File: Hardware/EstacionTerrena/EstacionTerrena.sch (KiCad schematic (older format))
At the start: 10 parts, among them J1 5-1814832-1

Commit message: Corrección de librerías en PCB de estación terrena
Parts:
- removed J1: 5-1814832-1, SamacSys_Parts:5-1814832-1, symbol EstacionTerrena-rescue:5-1814832-1-SamacSys_Parts
- removed JP1: Jumper_NC_Dual, Jumper:SolderJumper-3_P1.3mm_Open_RoundedPad1.0x1.5mm_NumberLabels, symbol Device:Jumper_NC_Dual
- added J1: 5-1814832-1, 5-1814832-1, symbol SamacSys_Parts:5-1814832-1
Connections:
- wire segments 29 -> 25
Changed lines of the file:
@@
 EESchema Schematic File Version 4
 LIBS:EstacionTerrena-cache
-EELAYER 26 0
+EELAYER 29 0
 EELAYER END
 $Descr A4 11693 8268
@@
 $EndComp
 Wire Wire Line
-	7050 4050 6700 4050
-$Comp
-L EstacionTerrena-rescue:5-1814832-1-SamacSys_Parts J1
-U 1 1 5BEE5678
-P 7250 4050
-F 0 "J1" H 7491 4026 50  0000 L CNN
-F 1 "5-1814832-1" H 7491 3934 50  0000 L CNN
-F 2 "SamacSys_Parts:5-1814832-1" H 7650 4150 50  0001 L CNN
-F 3 "http://www.te.com/commerce/DocumentDelivery/DDEController?Action=srchrtrv&DocNm=1814832&DocType=Customer+Drawing&DocLang=English" H 7650 4050 50  0001 L CNN
-F 4 "SUBMINIATURE COAX" H 7650 3950 50  0001 L CNN "Description"
-F 5 "TE Connectivity" H 7650 3750 50  0001 L CNN "Manufacturer_Name"
-F 6 "5-1814832-1" H 7650 3650 50  0001 L CNN "Manufacturer Part Number"
-F 7 "1355074" H 7450 3550 50  0001 L CNN "RS Part Number"
-F 8 "http://uk.rs-online.com/web/p/products/1355074" H 7650 3450 50  0001 L CNN "RS Price/Stock"
-F 9 "70084637" H 7650 3350 50  0001 L CNN "Allied_Number"
-F 10 "https://www.alliedelec.com/te-connectivity-5-1814832-1/70084637/" H 7650 3250 50  0001 L CNN "Allied Price/Stock"
-F 11 "5-1814832-1" H 7650 3150 50  0001 L CNN "Arrow Part Number"
-F 12 "https://www.arrow.com/en/products/5-1814832-1/te-connectivity" H 7650 3050 50  0001 L CNN "Arrow Price/Stock"
-	1    7250 4050
-	1    0    0    -1
-$EndComp
-Wire Wire Line
 	7150 4250 7150 4300
 Wire Wire Line
@@
 	1    0    0    -1
 $EndComp
-$Comp
-L power:GND #PWR026
-U 1 1 5C00A55B
-P 6050 5050
-F 0 "#PWR026" H 6050 4800 50  0001 C CNN
-F 1 "GND" H 6055 4877 50  0000 C CNN
-F 2 "" H 6050 5050 50  0001 C CNN
-F 3 "" H 6050 5050 50  0001 C CNN
-	1    6050 5050
-	1    0    0    -1
-$EndComp
 Wire Wire Line
 	5100 3950 5200 3950
@@
 $EndComp
 Wire Wire Line
-	5600 4250 6100 4250
-Wire Wire Line
 	5100 4250 5350 4250
 Wire Wire Line
@@
 Wire Wire Line
 	5200 3950 6100 3950
-$Comp
-L Device:Jumper_NC_Dual JP1
-U 1 1 5C2DD6B3
-P 5600 4950
-F 0 "JP1" H 5600 5096 50  0000 C CNN
-F 1 "Jumper_NC_Dual" H 5600 5187 50  0000 C CNN
-F 2 "Jumper:SolderJumper-3_P1.3mm_Open_RoundedPad1.0x1.5mm_NumberLabels" H 5600 4950 50  0001 C CNN
-F 3 "~" H 5600 4950 50  0001 C CNN
-	1    5600 4950
-	-1   0    0    1
-$EndComp
-Wire Wire Line
-	5350 4950 5350 4250
-Connection ~ 5350 4250
-Wire Wire Line
-	5600 4250 5600 4850
-Wire Wire Line
-	5850 4950 6050 4950
-Wire Wire Line
-	6050 4950 6050 5050
 Wire Wire Line
 	5100 4050 5250 4050
@@
 EndData
 $EndBitmap
+Wire Wire Line
+	5350 4250 6100 4250
+Connection ~ 5350 4250
+Wire Wire Line
+	7050 4050 6700 4050
+$Comp
+L SamacSys_Parts:5-1814832-1 J1
+U 1 1 5CCF549E
+P 7250 4050
+F 0 "J1" H 7494 4025 50  0000 L CNN
+F 1 "5-1814832-1" H 7494 3934 50  0000 L CNN
+F 2 "5-1814832-1" H 7650 4150 50  0001 L CNN
+F 3 "http://www.te.com/commerce/DocumentDelivery/DDEController?Action=srchrtrv&DocNm=1814832&DocType=Customer+Drawing&DocLang=English" H 7650 4050 50  0001 L CNN
+F 4 "SUBMINIATURE COAX" H 7650 3950 50  0001 L CNN "Description"
+F 5 "TE Connectivity" H 7650 3750 50  0001 L CNN "Manufacturer_Name"
+F 6 "5-1814832-1" H 7650 3650 50  0001 L CNN "Manufacturer Part Number"
+F 7 "1355074" H 7450 3550 50  0001 L CNN "RS Part Number"
+F 8 "http://uk.rs-online.com/web/p/products/1355074" H 7650 3450 50  0001 L CNN "RS Price/Stock"
+F 9 "70084637" H 7650 3350 50  0001 L CNN "Allied_Number"
+F 10 "https://www.alliedelec.com/te-connectivity-5-1814832-1/70084637/" H 7650 3250 50  0001 L CNN "Allied Price/Stock"
+F 11 "5-1814832-1" H 7650 3150 50  0001 L CNN "Arrow Part Number"
+F 12 "https://www.arrow.com/en/products/5-1814832-1/te-connectivity" H 7650 3050 50  0001 L CNN "Arrow Price/Stock"
+	1    7250 4050
+	1    0    0    -1
+$EndComp
 $EndSCHEMATC

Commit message: Estacion terrena:
- Nuevo LDO de 500mA para poder utilizar el CC1190 a toda su potencia de ser necesario
- Cambiado el MCP2210 por un PIC18F14K50 ya que el MCP2210 es MUY lento para transferencias SPI
- Agregado de footprints faltantes
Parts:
- J1: footprint 5-1814832-1 -> SamacSys_Parts:5-1814832-1
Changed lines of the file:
@@
 F 0 "J1" H 7494 4025 50  0000 L CNN
 F 1 "5-1814832-1" H 7494 3934 50  0000 L CNN
-F 2 "5-1814832-1" H 7650 4150 50  0001 L CNN
+F 2 "SamacSys_Parts:5-1814832-1" H 7650 4150 50  0001 L CNN
 F 3 "http://www.te.com/commerce/DocumentDelivery/DDEController?Action=srchrtrv&DocNm=1814832&DocType=Customer+Drawing&DocLang=English" H 7650 4050 50  0001 L CNN
 F 4 "SUBMINIATURE COAX" H 7650 3950 50  0001 L CNN "Description"

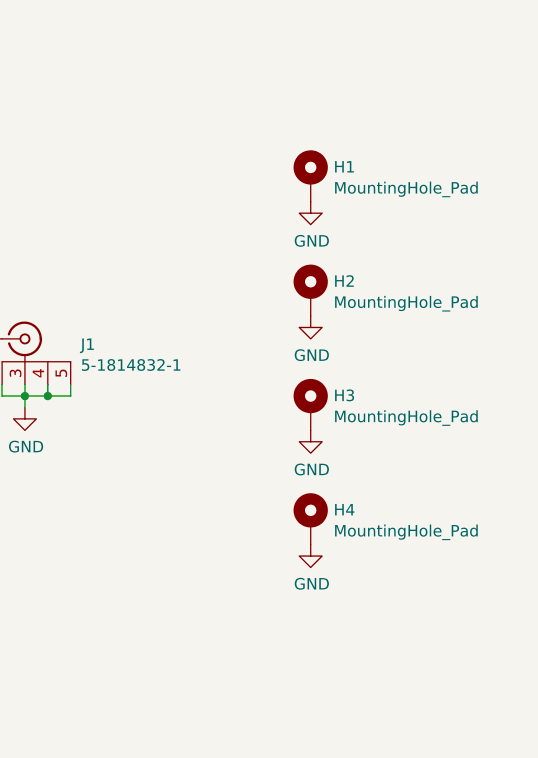
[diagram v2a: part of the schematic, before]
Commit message: Nuevo PCB de estación terrena con CC1190
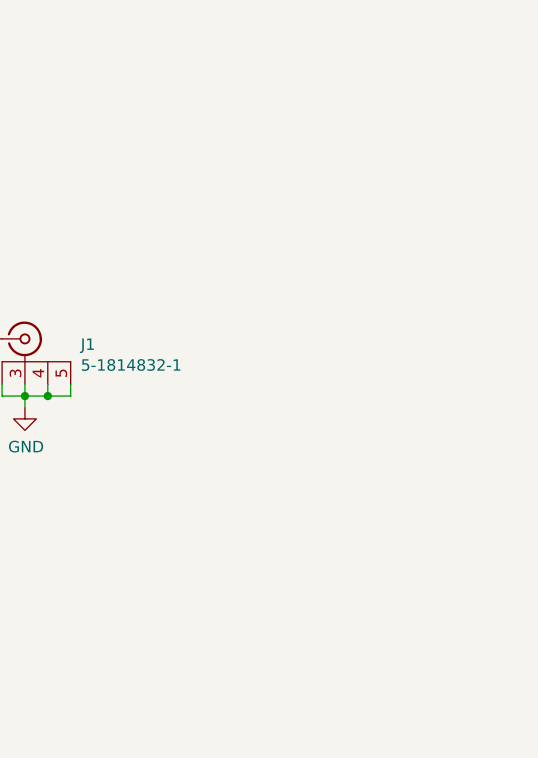
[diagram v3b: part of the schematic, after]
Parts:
- removed H1, H2, H3, H4: MountingHole_Pad, MountingHole:MountingHole_3.2mm_M3_Pad, symbol Mechanical:MountingHole_Pad
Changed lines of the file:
@@
 	7250 4350 7250 4300
-$Comp
-L Mechanical:MountingHole_Pad H1
-U 1 1 5BBFD953
-P 8500 3350
-F 0 "H1" H 8600 3401 50  0000 L CNN
-F 1 "MountingHole_Pad" H 8600 3309 50  0000 L CNN
-F 2 "MountingHole:MountingHole_3.2mm_M3_Pad" H 8500 3350 50  0001 C CNN
-F 3 "~" H 8500 3350 50  0001 C CNN
-	1    8500 3350
-	1    0    0    -1
-$EndComp
-$Comp
-L Mechanical:MountingHole_Pad H2
-U 1 1 5BBFDA3A
-P 8500 3850
-F 0 "H2" H 8600 3901 50  0000 L CNN
-F 1 "MountingHole_Pad" H 8600 3809 50  0000 L CNN
-F 2 "MountingHole:MountingHole_3.2mm_M3_Pad" H 8500 3850 50  0001 C CNN
-F 3 "~" H 8500 3850 50  0001 C CNN
-	1    8500 3850
-	1    0    0    -1
-$EndComp
-$Comp
-L Mechanical:MountingHole_Pad H3
-U 1 1 5BBFDA66
-P 8500 4350
-F 0 "H3" H 8600 4401 50  0000 L CNN
-F 1 "MountingHole_Pad" H 8600 4309 50  0000 L CNN
-F 2 "MountingHole:MountingHole_3.2mm_M3_Pad" H 8500 4350 50  0001 C CNN
-F 3 "~" H 8500 4350 50  0001 C CNN
-	1    8500 4350
-	1    0    0    -1
-$EndComp
-$Comp
-L Mechanical:MountingHole_Pad H4
-U 1 1 5BBFDA96
-P 8500 4850
-F 0 "H4" H 8600 4901 50  0000 L CNN
-F 1 "MountingHole_Pad" H 8600 4809 50  0000 L CNN
-F 2 "MountingHole:MountingHole_3.2mm_M3_Pad" H 8500 4850 50  0001 C CNN
-F 3 "~" H 8500 4850 50  0001 C CNN
-	1    8500 4850
-	1    0    0    -1
-$EndComp
-$Comp
-L power:GND #PWR0101
-U 1 1 5BBFDACC
-P 8500 3450
-F 0 "#PWR0101" H 8500 3200 50  0001 C CNN
-F 1 "GND" H 8505 3277 50  0000 C CNN
-F 2 "" H 8500 3450 50  0001 C CNN
-F 3 "" H 8500 3450 50  0001 C CNN
-	1    8500 3450
-	1    0    0    -1
-$EndComp
-$Comp
-L power:GND #PWR0102
-U 1 1 5BBFDAE9
-P 8500 3950
-F 0 "#PWR0102" H 8500 3700 50  0001 C CNN
-F 1 "GND" H 8505 3777 50  0000 C CNN
-F 2 "" H 8500 3950 50  0001 C CNN
-F 3 "" H 8500 3950 50  0001 C CNN
-	1    8500 3950
-	1    0    0    -1
-$EndComp
-$Comp
-L power:GND #PWR0103
-U 1 1 5BBFDB80
-P 8500 4450
-F 0 "#PWR0103" H 8500 4200 50  0001 C CNN
-F 1 "GND" H 8505 4277 50  0000 C CNN
-F 2 "" H 8500 4450 50  0001 C CNN
-F 3 "" H 8500 4450 50  0001 C CNN
-	1    8500 4450
-	1    0    0    -1
-$EndComp
-$Comp
-L power:GND #PWR0104
-U 1 1 5BBFDB9D
-P 8500 4950
-F 0 "#PWR0104" H 8500 4700 50  0001 C CNN
-F 1 "GND" H 8505 4777 50  0000 C CNN
-F 2 "" H 8500 4950 50  0001 C CNN
-F 3 "" H 8500 4950 50  0001 C CNN
-	1    8500 4950
-	1    0    0    -1
-$EndComp
 $Comp
 L Graphic:Logo_Open_Hardware_Large #LOGO1
